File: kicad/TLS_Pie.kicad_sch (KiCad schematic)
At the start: 23 parts, among them M1 stepper + 50:1, U1 DS3231 breakout, U10 fan 5 V, U11 INA226 -- NOT FITTED, U12 BCD5A -> 16.8 V / 1.5 A (17.0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, U3 LM2596S-ADJ -> 5.1 V, U4 Big Easy Driver, U7 VLP-16 interface box, U8 Velodyne VLP-16

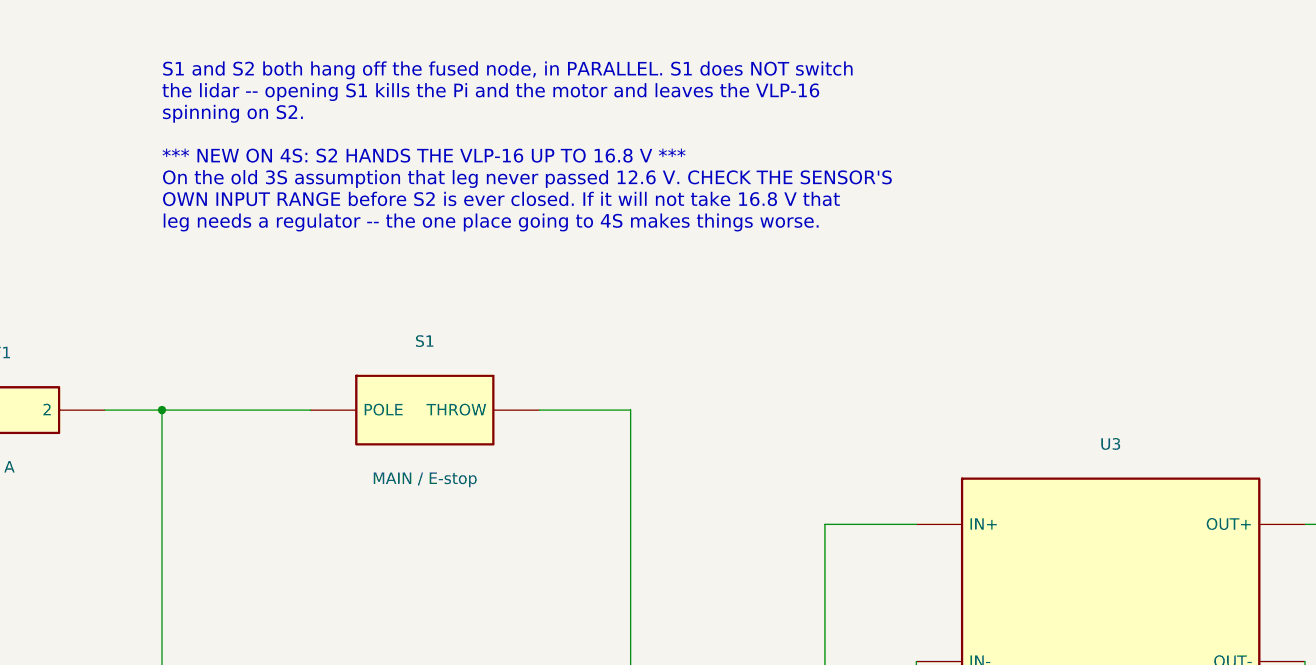
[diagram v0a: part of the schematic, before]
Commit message: VLP-16 voltage settled from the datasheets: 16.8 V is inside its range
This was the last electrical blocker and it is closed.  Velodyne quote 9-32
VDC with the interface box; the user manual carries a narrower 9-18 V.  16.8 V
is inside BOTH, so the conservative reading still passes, and the pack cannot
exceed 16.8 V anyway because the BMS cuts off at 4.2 V/cell.  No regulator is
needed on S2.

Recording both figures rather than picking one.  They disagree and the
disagreement is probably sensor-alone versus with-the-box, but the decision
does not turn on it -- so the honest record keeps both and notes that the
narrower one still clears.

Two things the hunt turned up that do matter and were not being tracked:

  * the supply must source up to 3.0 A for rotor spin-up, though the sensor
    runs on ~8 W.  That surge stacks on everything else the rig draws, so peak
    can approach F1's 6 A.  If F1 ever blows at switch-on with nothing faulty,
    that is the reason.
  * the barrel jack is 5.5 mm OD x 2.5 mm ID centre positive -- a 2.5 mm pin,
    NOT the 2.1 mm a PJ-102A plug carries, which is what the sheet said.  A
    2.1 mm plug in a 2.5 mm socket grips nothing and goes intermittent.

Verified: 2186 validator checks 0 failed; KiCad ERC 0 violations.

Co-Authored-By: Claude Opus 5 <noreply@anthropic.com>
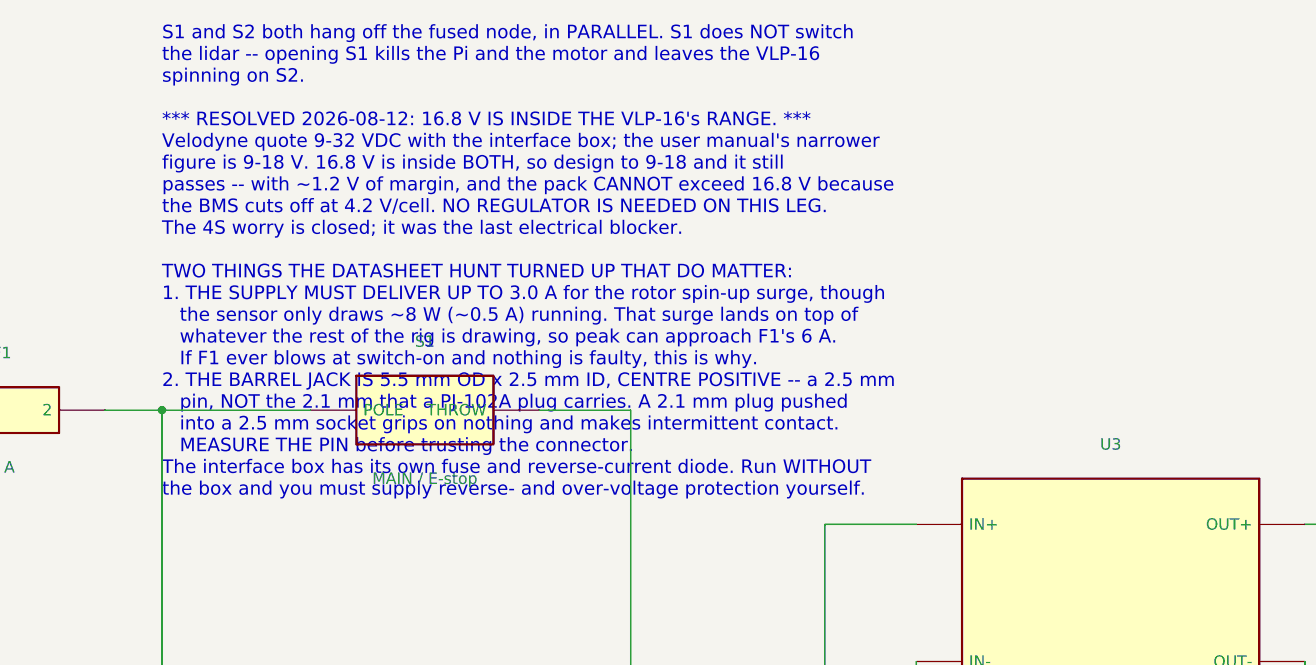
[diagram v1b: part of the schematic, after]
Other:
- note added: "S1 and S2 both hang off the fused node, in PARALLEL. S1 does NOT switch the lidar -- opening S1 kills the Pi and the motor and leaves the VLP-16 spinning on S2. *** RESOLVED 2026-08-12: 16.8 V IS INSIDE THE VLP-16's RANGE. *** Velodyne quote 9-32 VDC with the interface box; the user manual's narrower figure is 9-18 V. 16.8 V is inside BOTH, so design to 9-18 and it still passes -- with ~1.2 V of 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"
- note removed: "S1 and S2 both hang off the fused node, in PARALLEL. S1 does NOT switch the lidar -- opening S1 kills the Pi and the motor and leaves the VLP-16 spinning on S2. *** NEW ON 4S: S2 HANDS THE VLP-16 UP TO 16.8 V *** On the old 3S assumption that leg never passed 12.6 V. CHECK THE SENSOR'S OWN INPUT RANGE before S2 is ever closed. If it will not take 16.8 V that leg needs a regulator -- the one place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"
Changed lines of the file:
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@@
   (wire (pts (xy 481.33 99.06) (xy 524.51 99.06)) (stroke (width 0) (type default)))
   (wire (pts (xy 524.51 99.06) (xy 524.51 86.36)) (stroke (width 0) (type default)))
-  (text "S1 and S2 both hang off the fused node, in PARALLEL. S1 does NOT switch\nthe lidar -- opening S1 kills the Pi and the motor and leaves the VLP-16\nspinning on S2.\n\n*** NEW ON 4S: S2 HANDS THE VLP-16 UP TO 16.8 V ***\nOn the old 3S assumption that leg never passed 12.6 V. CHECK THE SENSOR'S\nOWN INPUT RANGE before S2 is ever closed. If it will not take 16.8 V that\nleg needs a regulator -- the one place going to 4S makes things worse." (exclude_from_sim yes) (at 196.85 29.245 0) (effects (font (size 1.5 1.5)) (justify left)))
+  (text "S1 and S2 both hang off the fused node, in PARALLEL. S1 does NOT switch\nthe lidar -- opening S1 kills the Pi and the motor and leaves the VLP-16\nspinning on S2.\n\n*** RESOLVED 2026-08-12: 16.8 V IS INSIDE THE VLP-16's RANGE. ***\nVelodyne quote 9-32 VDC with the interface box; the user manual's narrower\nfigure is 9-18 V. 16.8 V is inside BOTH, so design to 9-18 and it still\npasses -- with ~1.2 V of margin, and the pack CANNOT exceed 16.8 V because\nthe BMS cuts off at 4.2 V/cell. NO REGULATOR IS NEEDED ON THIS LEG.\nThe 4S worry is closed; it was the last electrical blocker.\n\nTWO THINGS THE DATASHEET HUNT TURNED UP THAT DO MATTER:\n1. THE SUPPLY MUST DELIVER UP TO 3.0 A for the rotor spin-up surge, though\n   the sensor only draws ~8 W (~0.5 A) running. That surge lands on top of\n   whatever the rest of the rig is drawing, so peak can approach F1's 6 A.\n   If F1 ever blows at switch-on and nothing is faulty, this is why.\n2. THE BARREL JACK IS 5.5 mm OD x 2.5 mm ID, CENTRE POSITIVE -- a 2.5 mm\n   pin, NOT the 2.1 mm that a PJ-102A plug carries. A 2.1 mm plug pushed\n   into a 2.5 mm socket grips on nothing and makes intermittent contact.\n   MEASURE THE PIN before trusting the connector.\nThe interface box has its own fuse and reverse-current diode. Run WITHOUT\nthe box and you must supply reverse- and over-voltage protection yourself." (exclude_from_sim yes) (at 196.85 42.015 0) (effects (font (size 1.5 1.5)) (justify left)))
   (text "CONNECT THE TAPS IN THIS ORDER:  0V  4.2V  8.4V  12.6V  16.8V\nThe board names its pads by voltage, and those are FULL-CHARGE values --\nNOT what a flat pack measures. Against 0V at the measured 12.24 V total you\nshould read roughly:   0 / 3.06 / 6.12 / 9.18 / 12.24 V.\nWHAT MATTERS IS THE ORDER, evenly spaced and ascending. Meter every tap on\nthe free connector BEFORE plugging it in.\nThe protection ICs are powered from the taps. Out of order, one stage sees\nmost of the pack across single-cell inputs and dies silently -- leaving a\nboard that looks fine and protects nothing. Solder all five to the pack\nFIRST, meter the free connector, and only then plug it in.\n\n4.2V/8.4V/12.6V carry milliamps -- 22-24 AWG.  16.8V (B+) and 0V (B-) carry\nthe FULL pack current -- run those two THICK. Check the 16.8V lead: it is\nthe one that looks like a balance wire and is not.\n\n*** PAD ADJACENCY ON THE REAL BOARD -- ONE SLIP IS A FIRE ***\nRight edge, top to bottom:  16.8V | (+) | (-) | 4.2V.\n  (+) beside 16.8V   -- a bridge here is HARMLESS. They are the same copper:\n                        the ten FETs are all in the NEGATIVE leg, so the\n                        positive is never switched. MEASURED 0 ohms on the\n                        board 2026-08-11 -- this is verified, not inferred.\n  (-) beside 4.2V    -- a bridge here is the WORST SHORT ON THE BOARD. (-) is\n                        pack negative through the FETs and 4.2V is the top of\n                        group 1, so a stray strand puts a DEAD SHORT ACROSS\n                        THREE PARALLEL CELLS. No fuse is in that path and\n                        nothing protects it. Sleeve it, inspect it, and work\n                        that corner one lead at a time.\nLeave the CD and FD test pads alone." (exclude_from_sim yes) (at 34.29 160.155 0) (effects (font (size 1.5 1.5)) (justify left)))
   (text "PANEL METER PM1 -- and it changes the ground topology, so read this.\n\nITS THICK PAIR IS THE SHUNT, AND THE SHUNT IS IN THE NEGATIVE LEG. So it\ngoes in the RETURN, between the rig's ground and P- -- NOT in the +VBATT\nrail where U11 goes. GND and P- are now separate nodes joined ONLY through\nPM1. They cross twice on this sheet with no junction dot and are NOT\nconnected there. Bridge them anywhere and you short out the shunt: the\nmeter reads 0.00 A for ever and nothing warns you.\n\n*** VERIFY THE SHUNT LEG BEFORE SOLDERING ***\nMeter resistance thin-black to thick-black. NEAR ZERO = negative-leg shunt\nand this drawing is right. If instead thin-RED reads near zero to a thick\nlead, the shunt is in the POSITIVE leg -- then it belongs where U11 is, in\nthe +VBATT rail, and this corner of the sheet must be redrawn.\nThe two thick leads should read a fraction of an ohm to each other: that\nIS the shunt.\n\nTHIN BLACK GOES TO THE SAME SIDE AS THICK BLACK (P-). On most of these the\ntwo blacks are common inside the meter, so putting the thin one on the rig\nside of the shunt bridges it -- the same silent zero-amps failure.\n\nSUPPLY FROM +VSW1, NOT +VBATT. These meters draw ~20 mA continuously. On\n+VBATT that is ~0.5 Ah/day and would flatten this ~9 Ah pack in about three\nweeks of standing -- which is how it got flat the first time. On +VSW1 it\ndies with S1. VSENSE still reads TRUE PACK VOLTS because it taps +VBATT\nupstream of the switch, and it draws only microamps through its divider.\n\nReads 0.00 A while charging with S1 and S2 open. Correct: the charge return\nis on the pack side of the shunt, so charge current never crosses it.\nIts two thick leads carry the WHOLE rig's return -- mount PM1 at the BMS and\nkeep them short and heavy. The 6 A fuse is what keeps this inside its 10 A." (exclude_from_sim yes) (at 196.85 241.43 0) (effects (font (size 1.3 1.3)) (justify left)))
@@
       (effects (font (size 1.27 1.27)))
     )
-    (property "Description" "Barrel jack PJ-102A, centre positive. TB1 carries the sensor's factory cable"
+    (property "Description" "VLP-16 interface box. 9-32 VDC per the spec sheet, 9-18 V per the user manual -- 16.8 V is inside both, so no regulator is needed on S2. Barrel jack is 5.5 mm OD x 2.5 mm ID CENTRE POSITIVE (2.5, not the 2.1 a PJ-102A plug carries -- measure it). Supply must source 3.0 A for rotor spin-up though the sensor runs on ~8 W. Has its own fuse and reverse-current diode. TB1 carries the sensor's factory cable"
       (at 439.42 245.11 0)
       (hide yes)
